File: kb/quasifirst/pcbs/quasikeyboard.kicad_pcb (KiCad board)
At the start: 2 copper layers, 122 x 93.1 mm, 21 parts

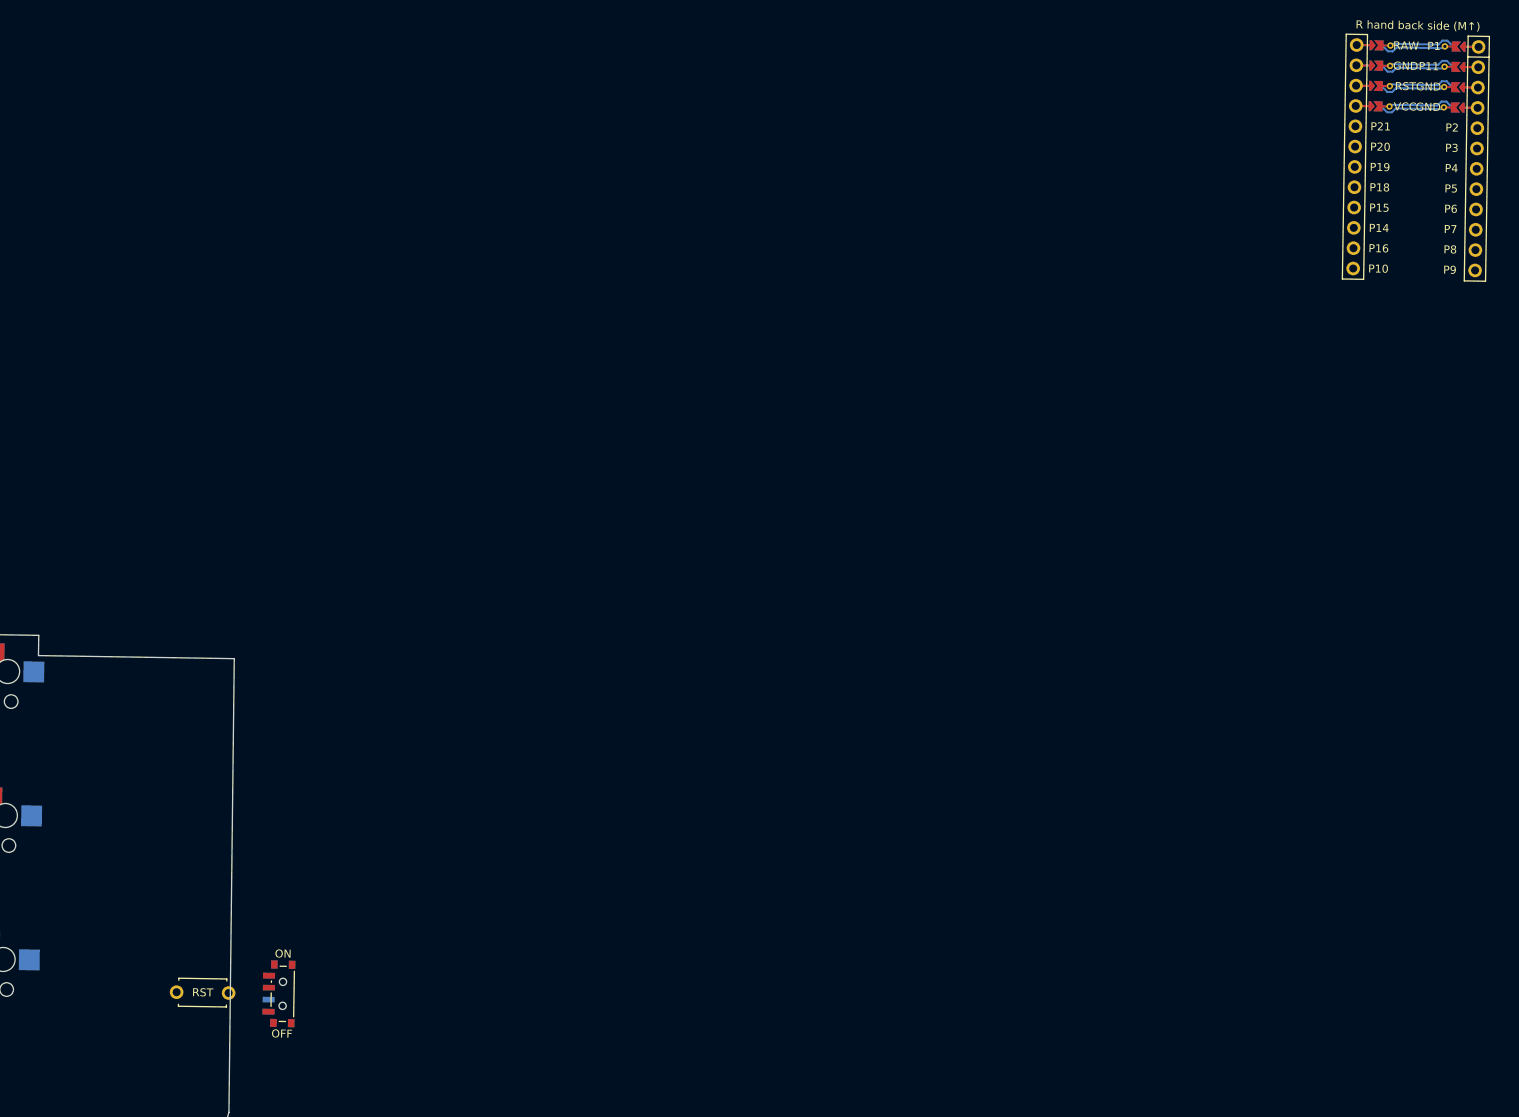
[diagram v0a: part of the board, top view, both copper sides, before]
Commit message: adding components and refining placements and connections
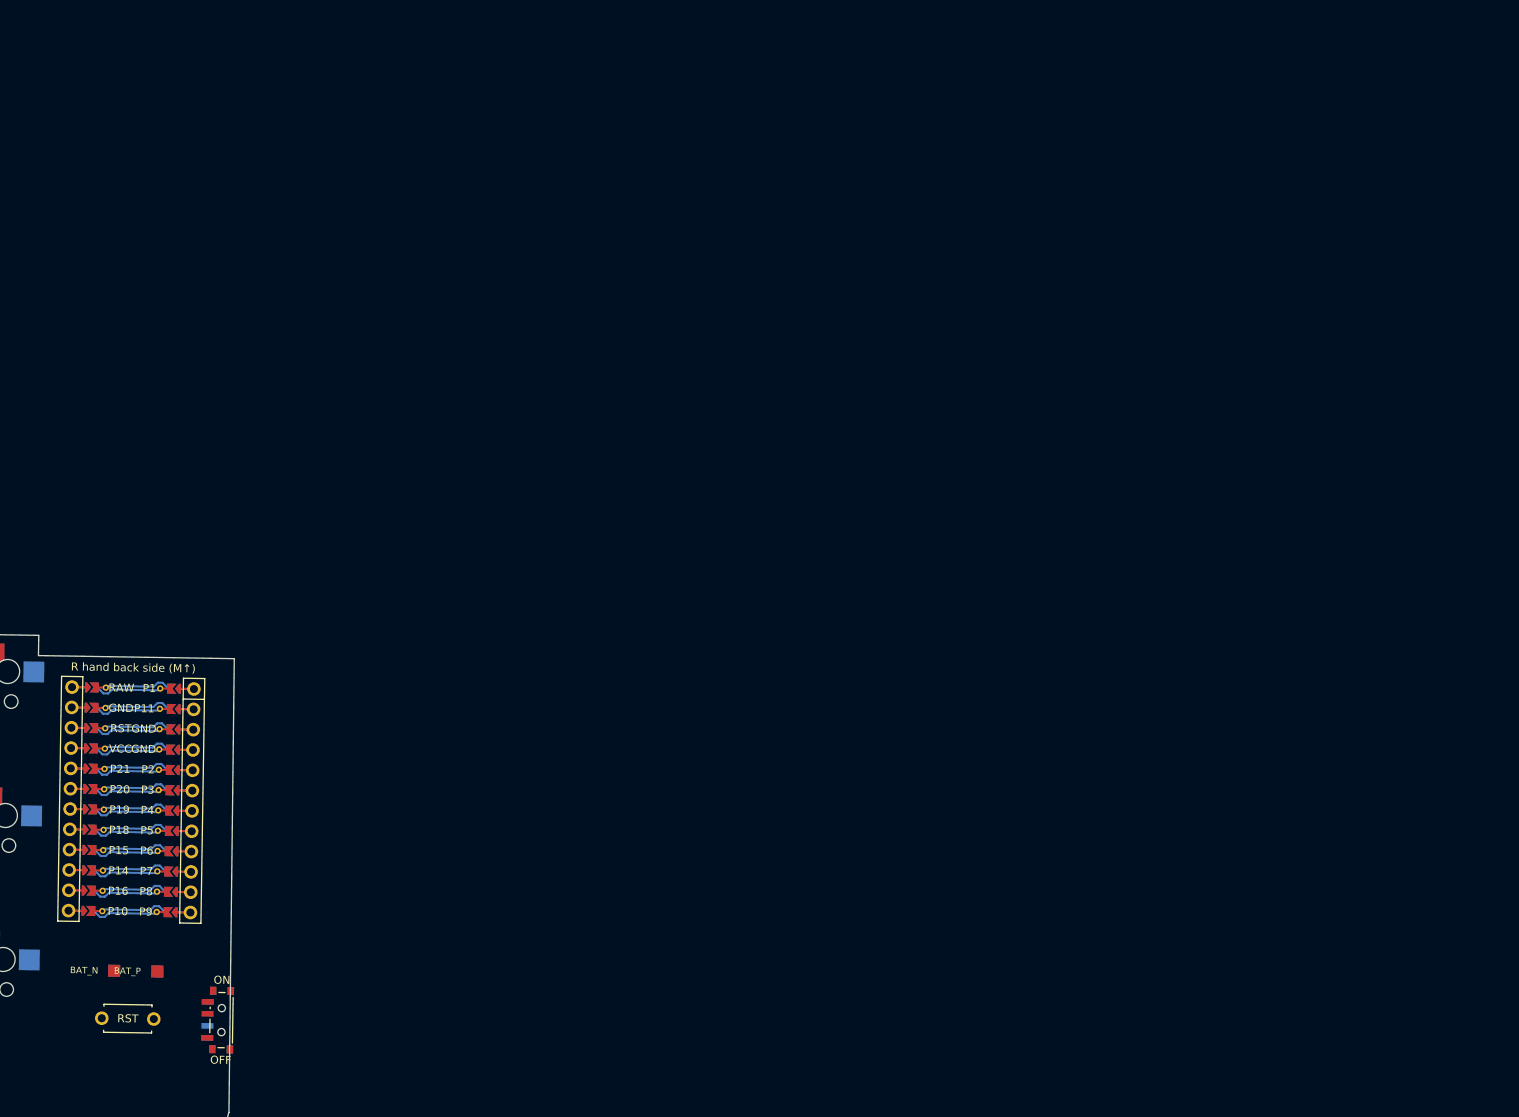
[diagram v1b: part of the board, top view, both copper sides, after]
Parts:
- added PAD1: , SMDPad, F.Cu at (264.7, 149.5)
- added PAD2: , SMDPad, F.Cu at (270.1, 149.6)
- moved MCU1 179.5 mm to (266.9, 126.9)
- moved RST1 9.90 mm to (266.4, 155.5)
- moved PWR1 8.33 mm to (278.1, 155.7)
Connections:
- MCU1 pad 10: matrix_pinky_top -> MCU1_10
- MCU1 pad 11: thumb_middle -> MCU1_11
- MCU1 pad 12: thumb_reachy -> MCU1_12
- MCU1 pad 13: matrix_index_home -> MCU1_13
- MCU1 pad 14: matrix_middle_home -> MCU1_14
- MCU1 pad 15: matrix_ring_home -> MCU1_15
- MCU1 pad 16: matrix_pinky_home -> MCU1_16
- MCU1 pad 17: matrix_ring_top -> MCU1_17
- MCU1 pad 18: matrix_middle_top -> MCU1_18
- MCU1 pad 19: matrix_index_top -> MCU1_19
- MCU1 pad 20: matrix_inner_top -> MCU1_20
- MCU1 pad 5: matrix_pinky_bottom -> MCU1_5
- MCU1 pad 6: matrix_ring_bottom -> MCU1_6
- MCU1 pad 7: matrix_middle_bottom -> MCU1_7
- MCU1 pad 8: matrix_index_bottom -> MCU1_8
- MCU1 pad 9: matrix_inner_bottom -> MCU1_9
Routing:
- net (no net): track 112.6 -> 337.7 mm

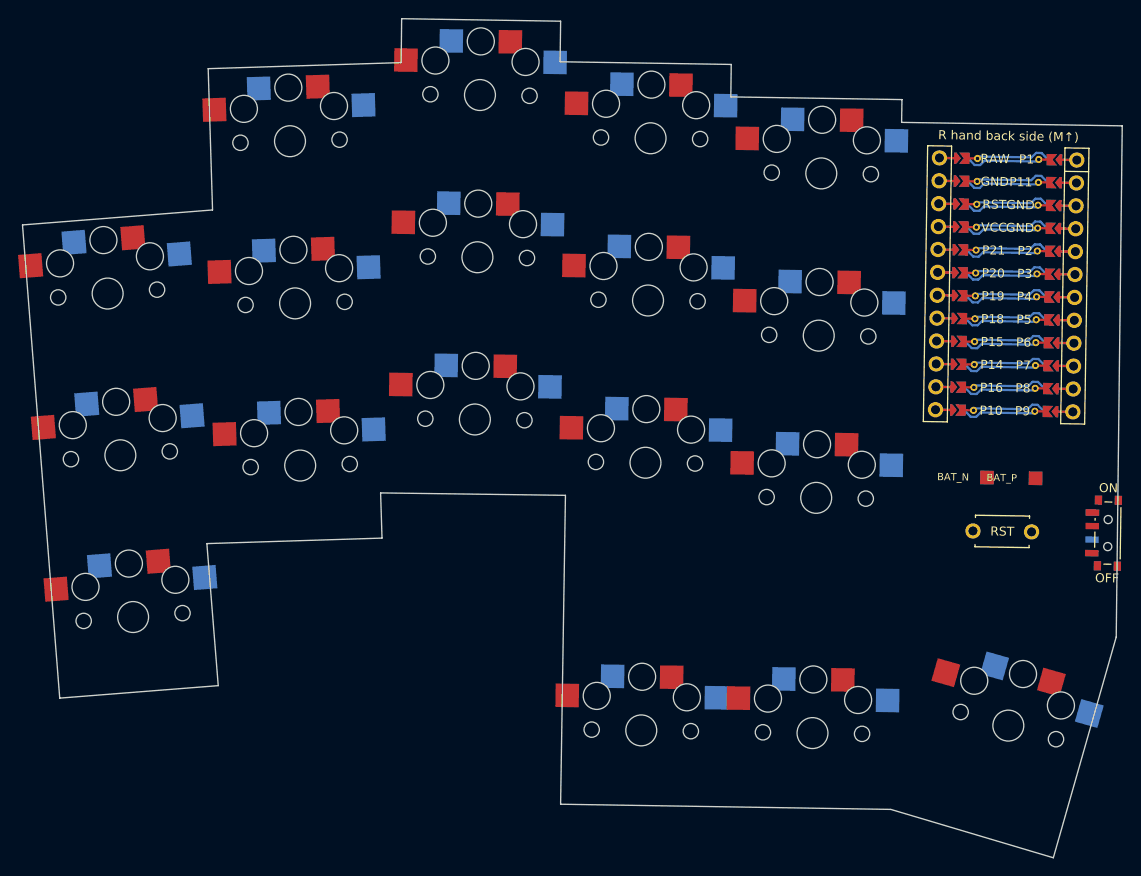
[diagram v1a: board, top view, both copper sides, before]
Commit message: swapped chocs for ceoloide ones, reworked nets a bit, started to improve board layout, flipped thumb switch
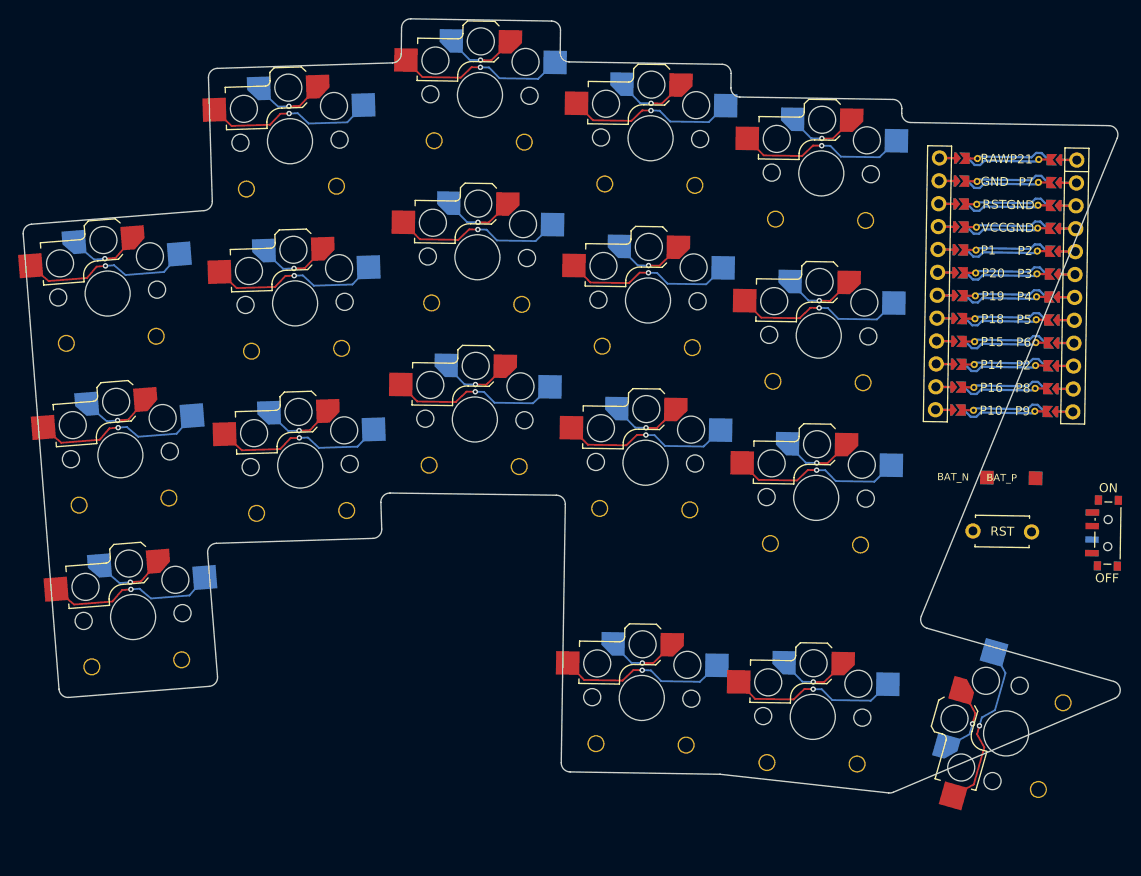
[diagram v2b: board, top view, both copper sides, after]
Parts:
- S1, S10, S11, S12, S13, S14, S15, S16, S17, S18, S2, S3, S4, S5, S6, S7, S8, S9: footprint PG1350 -> ceoloide:switch_choc_v1_v2; moved to B.Cu
- moved S16 3.60 mm to (226.4, 174.0)
- moved S17 1.80 mm to (245.4, 176.1)
- moved S18 0.90 mm to (266.9, 177.9), turned to 74.1 degrees
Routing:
- net GND: track 0.00 -> 343.1 mm, vias 0 -> 18
- net matrix_ring_top: track 0.00 -> 8.27 mm, vias 0 -> 1
- net matrix_ring_home: track 0.00 -> 8.27 mm, vias 0 -> 1
- net matrix_ring_bottom: track 0.00 -> 8.27 mm, vias 0 -> 1
- net thumb_reachy: track 0.00 -> 8.27 mm, vias 0 -> 1
- net matrix_pinky_top: track 0.00 -> 8.27 mm, vias 0 -> 1
- net matrix_pinky_home: track 0.00 -> 8.27 mm, vias 0 -> 1
- net matrix_pinky_bottom: track 0.00 -> 8.27 mm, vias 0 -> 1
- net thumb_middle: track 0.00 -> 8.27 mm, vias 0 -> 1
- net thumb_innit: track 0.00 -> 8.27 mm, vias 0 -> 1
- net matrix_middle_bottom: track 0.00 -> 8.27 mm, vias 0 -> 1
- net matrix_inner_bottom: track 0.00 -> 8.27 mm, vias 0 -> 1
- net matrix_index_bottom: track 0.00 -> 8.27 mm, vias 0 -> 1
- net matrix_inner_home: track 0.00 -> 8.27 mm, vias 0 -> 1
- net matrix_middle_top: track 0.00 -> 8.27 mm, vias 0 -> 1
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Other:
- board size 122 x 93.1 mm -> 121.7 x 85.9 mm

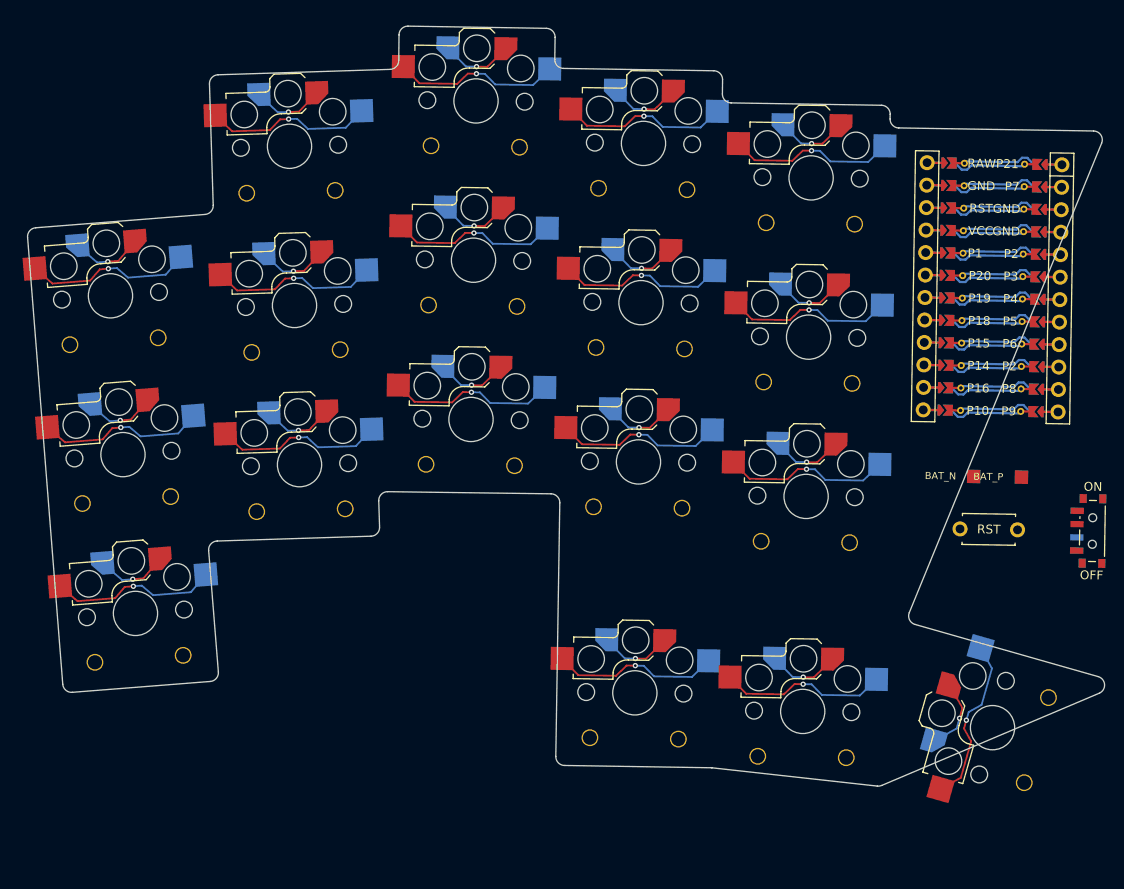
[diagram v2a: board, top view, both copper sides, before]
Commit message: desing phase should be over, might have to come back with tweaks now that will start trace routing
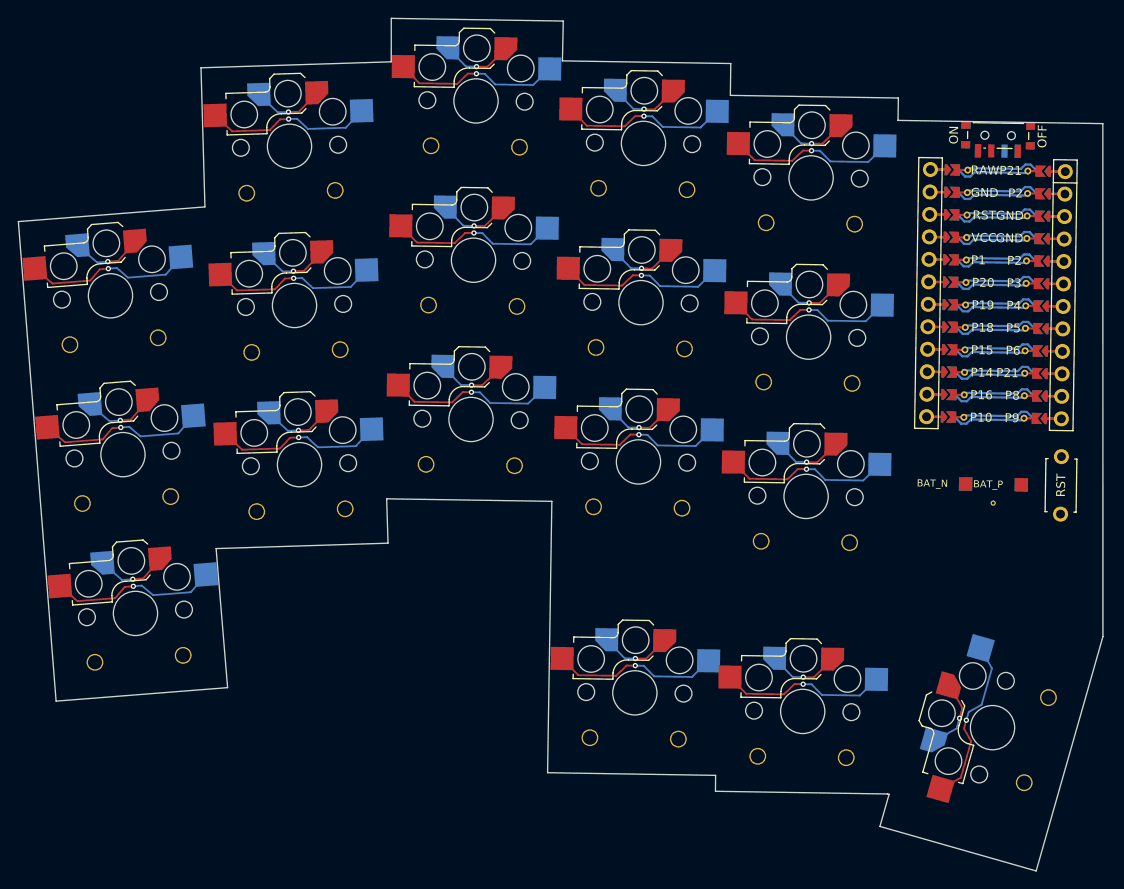
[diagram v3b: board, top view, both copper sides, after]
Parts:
- added REF**: VIA-0.6mm, VIA-0.6mm, F.Cu at (266.9, 152.5)
- moved PWR1 45.9 mm to (267.5, 111.0), turned to 89.1 degrees
- moved RST1 9.56 mm to (274.6, 150.5), turned to 89.1 degrees
- moved PAD1 1.24 mm to (263.8, 150.4)
- moved MCU1 0.86 mm to (267.3, 127.7)
- moved PAD2 0.85 mm to (270.1, 150.5)
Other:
- board size 121.7 x 85.9 mm -> 122.6 x 96.3 mm

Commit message: stuck on figuring out the right pins
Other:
- board size 122.6 x 96.3 mm -> 122.5 x 96.3 mm
